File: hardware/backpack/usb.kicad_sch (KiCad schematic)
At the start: 8 parts, among them U3 USB3343

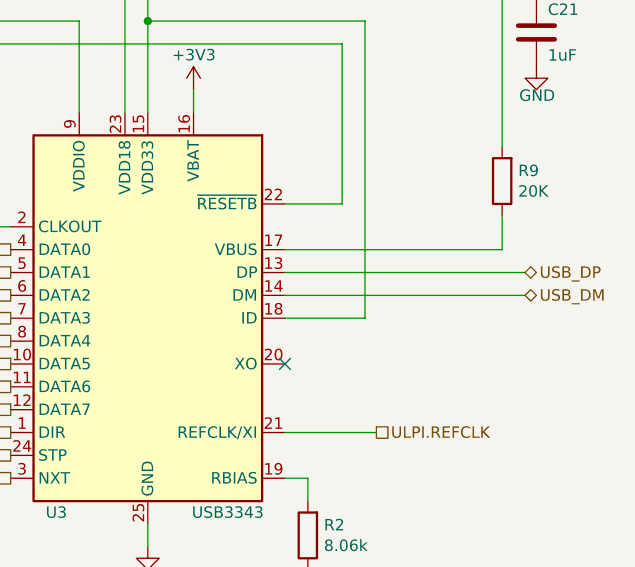
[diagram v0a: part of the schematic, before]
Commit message: connections + placement done
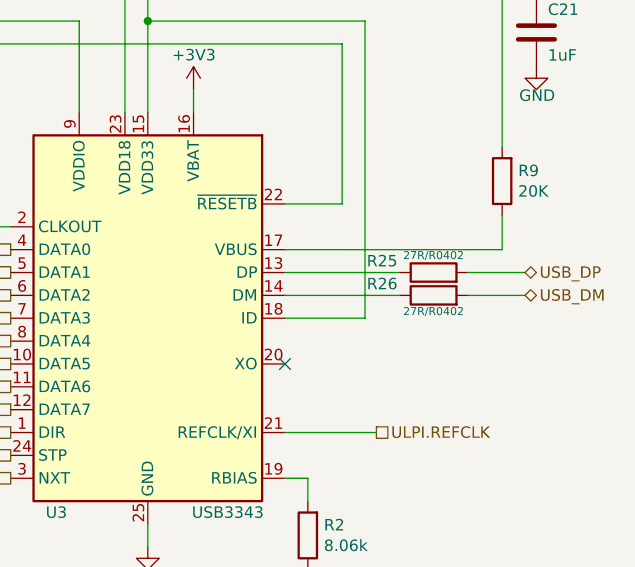
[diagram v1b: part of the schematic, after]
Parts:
- added R25, R26: 27R/R0402, Resistor_SMD:R_0402_1005Metric, symbol OLIMEX_RCL:R
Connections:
- net USB_DM: now also R26.2; no longer U3.14 (DM)
- net USB_DP: now also R25.2; no longer U3.13 (DP)
- new net: R25.1, U3.13 (DP)
- new net: R26.1, U3.14 (DM)
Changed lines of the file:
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@@
+	(wire
+		(pts
+			(xy 204.47 92.71) (xy 210.82 92.71)
+		)
+		(stroke
+			(width 0)
+			(type default)
+		)
+	)
 	(wire
 		(pts
@@
 	(wire
 		(pts
-			(xy 184.15 92.71) (xy 210.82 92.71)
-		)
-		(stroke
-			(width 0)
-			(type solid)
-		)
-	)
-	(wire
-		(pts
 			(xy 127 62.23) (xy 149.86 62.23)
 		)
@@
 	(wire
 		(pts
-			(xy 184.15 90.17) (xy 210.82 90.17)
+			(xy 184.15 92.71) (xy 196.85 92.71)
 		)
 		(stroke
@@
 	(wire
 		(pts
+			(xy 204.47 90.17) (xy 210.82 90.17)
+		)
+		(stroke
+			(width 0)
+			(type default)
+		)
+	)
+	(wire
+		(pts
 			(xy 176.53 43.18) (xy 176.53 44.45)
 		)
@@
 			(width 0)
 			(type solid)
+		)
+	)
+	(wire
+		(pts
+			(xy 184.15 90.17) (xy 196.85 90.17)
+		)
+		(stroke
+			(width 0)
+			(type default)
 		)
 	)
@@
 	)
 	(symbol
+		(lib_id "OLIMEX_RCL:R")
+		(at 200.66 90.17 0)
+		(unit 1)
+		(exclude_from_sim yes)
+		(in_bom yes)
+		(on_board yes)
+		(dnp no)
+		(property "Reference" "R25"
+			(at 194.945 88.9 0)
+			(effects
+				(font
+					(size 1.27 1.27)
+				)
+			)
+		)
+		(property "Value" "27R/R0402"
+			(at 200.66 88.265 0)
+			(effects
+				(font
+					(size 0.889 0.889)
+				)
+			)
+		)
+		(property "Footprint" "Resistor_SMD:R_0402_1005Metric"
+			(at 200.66 91.948 0)
+			(effects
+				(font
+					(size 0.762 0.762)
+				)
+				(hide yes)
+			)
+		)
+		(property "Datasheet" ""
+			(at 200.66 90.17 90)
+			(effects
+				(font
+					(size 0.762 0.762)
+				)
+			)
+		)
+		(property "Description" ""
+			(at 200.66 90.17 0)
+			(effects
+				(font
+					(size 1.27 1.27)
+				)
+				(hide yes)
+			)
+		)
+		(property "Fieldname 1" "Value 1"
+			(at 200.66 90.17 0)
+			(effects
+				(font
+					(size 1.524 1.524)
+				)
+				(hide yes)
+			)
+		)
+		(property "Fieldname2" "Value2"
+			(at 200.66 90.17 0)
+			(effects
+				(font
+					(size 1.524 1.524)
+				)
+				(hide yes)
+			)
+		)
+		(property "Fieldname3" "Value3"
+			(at 200.66 90.17 0)
+			(effects
+				(font
+					(size 1.524 1.524)
+				)
+				(hide yes)
+			)
+		)
+		(property "lcsc#" "C138021"
+			(at 200.66 90.17 0)
+			(effects
+				(font
+					(size 1.27 1.27)
+				)
+				(hide yes)
+			)
+		)
+		(pin "1"
+		)
+		(pin "2"
+		)
+		(instances
+			(project "backpack"
+				(path "/df6062c3-a570-4505-924c-c7fe32df3670/5f28fc0f-df6f-45b5-aac7-18a67e46504e"
+					(reference "R25")
+					(unit 1)
+				)
+			)
+		)
+	)
+	(symbol
 		(lib_id "Device:R")
 		(at 208.28 80.01 180)
@@
 					(unit 1)
 				)
+			)
+		)
+	)
+	(symbol
+		(lib_id "OLIMEX_RCL:R")
+		(at 200.66 92.71 0)
+		(unit 1)
+		(exclude_from_sim yes)
+		(in_bom yes)
+		(on_board yes)
+		(dnp no)
+		(property "Reference" "R26"
+			(at 194.945 91.44 0)
+			(effects
+				(font
+					(size 1.27 1.27)
+				)
+			)
+		)
+		(property "Value" "27R/R0402"
+			(at 200.66 94.488 0)
+			(effects
+				(font
+					(size 0.889 0.889)
+				)
+			)
+		)
+		(property "Footprint" "Resistor_SMD:R_0402_1005Metric"
+			(at 200.66 94.488 0)
+			(effects
+				(font
+					(size 0.762 0.762)
+				)
+				(hide yes)
+			)
+		)
+		(property "Datasheet" ""
+			(at 200.66 92.71 90)
+			(effects
+				(font
+					(size 0.762 0.762)
+				)
+			)
+		)
+		(property "Description" ""
+			(at 200.66 92.71 0)
+			(effects
+				(font
+					(size 1.27 1.27)
+				)
+				(hide yes)
+			)
+		)
+		(property "Fieldname 1" "Value 1"
+			(at 200.66 92.71 0)
+			(effects
+				(font
+					(size 1.524 1.524)
+				)
+				(hide yes)
+			)
+		)
+		(property "Fieldname2" "Value2"
+			(at 200.66 92.71 0)
+			(effects
+				(font
+					(size 1.524 1.524)
+				)
+				(hide yes)
+			)
+		)
+		(property "Fieldname3" "Value3"
+			(at 200.66 92.71 0)
+			(effects
+				(font
+					(size 1.524 1.524)
+				)
+				(hide yes)
+			)
+		)
+		(property "lcsc#" "C138021"
+			(at 200.66 92.71 0)
+			(effects
+				(font
+					(size 1.27 1.27)
+				)
+				(hide yes)
+			)
+		)
+		(pin "1"
+		)
+		(pin "2"
+		)
+		(instances
+			(project "backpack"
+				(path "/df6062c3-a570-4505-924c-c7fe32df3670/5f28fc0f-df6f-45b5-aac7-18a67e46504e"
+					(reference "R26")
+					(unit 1)
+				)

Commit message: updates before fab 04-04-24
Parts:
- C18: lcsc# C129131 -> C307331
- C19, C20, C21: lcsc# C106254 -> C52923
- R1: value 10k -> 10K; lcsc# C60490 -> C25744
- R25, R26: value 27R/R0402 -> 27R
- R9: lcsc# C93942 -> C25765
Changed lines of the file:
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@@
 			)
 		)
-		(property "lcsc#" "C106254"
+		(property "lcsc#" "C52923"
 			(at 176.53 48.26 0)
 			(effects
@@
 			)
 		)
-		(property "Value" "10k"
+		(property "Value" "10K"
 			(at 108.712 48.387 0)
 			(effects
@@
 			)
 		)
-		(property "lcsc#" "C60490"
+		(property "lcsc#" "C25744"
 			(at 110.49 49.53 0)
 			(effects
@@
 			)
 		)
-		(property "Value" "27R/R0402"
+		(property "Value" "27R"
 			(at 200.66 88.265 0)
 			(effects
@@
 			)
 		)
-		(property "Datasheet" ""
+		(property "Datasheet" "~"
 			(at 200.66 90.17 90)
 			(effects
@@
 			)
 		)
-		(property "lcsc#" "C93942"
+		(property "lcsc#" "C25765"
 			(at 208.28 80.01 0)
 			(effects
@@
 			)
 		)
-		(property "lcsc#" "C106254"
+		(property "lcsc#" "C52923"
 			(at 212.09 63.5 0)
 			(effects
@@
 			)
 		)
-		(property "Datasheet" "~"
+		(property "Datasheet" ""
 			(at 127 77.47 0)
 			(effects
@@
 			)
 		)
-		(property "lcsc#" "C129131"
+		(property "lcsc#" " C307331"
 			(at 127 77.47 0)
 			(effects
@@
 			)
 		)
-		(property "lcsc#" "C106254"
+		(property "lcsc#" "C52923"
 			(at 157.48 48.26 0)
 			(effects
@@
 			)
 		)
-		(property "Value" "27R/R0402"
+		(property "Value" "27R"
 			(at 200.66 94.488 0)
 			(effects
@@
 			)
 		)
-		(property "Datasheet" ""
+		(property "Datasheet" "~"
 			(at 200.66 92.71 90)
 			(effects
